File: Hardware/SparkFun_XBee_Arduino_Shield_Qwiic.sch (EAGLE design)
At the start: 76 parts, among them J4 QWIIC_RIGHT_ANGLE, Q1 220mA/50V/3.5Ω, Q3 3.1A/30V/105mΩ, Q5 20V/4.2A/52mΩ/1.4W, U1 FSUSB30MUX_MSOP10, U2 AP63203, U3 ESD Diode, U4 FT231XS, U5 ESD Diode, X1 JUMPER-SMT_2_NO_SILK

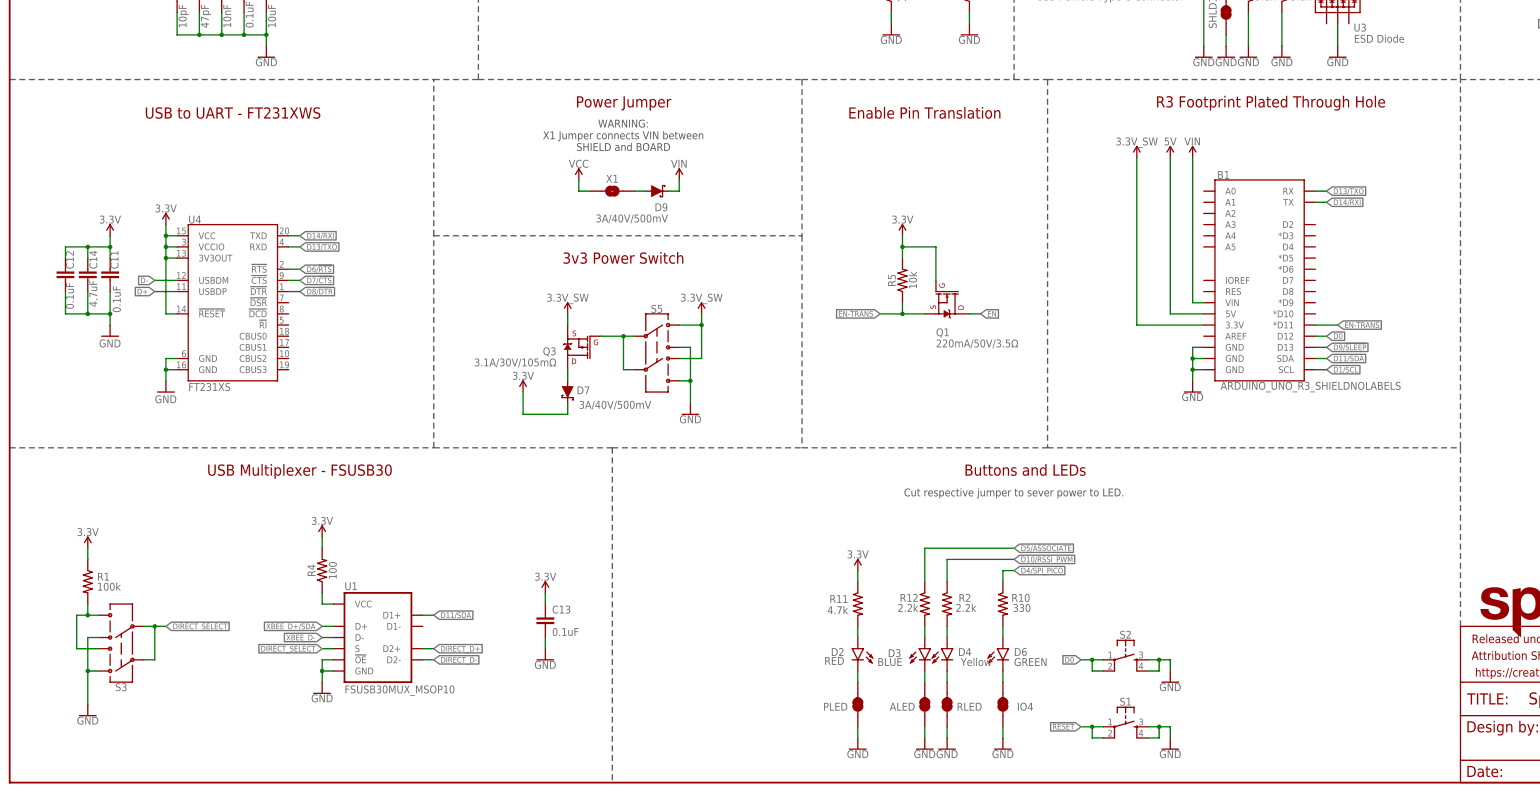
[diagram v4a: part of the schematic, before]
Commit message: Adds more measures and additional notes in the schematic
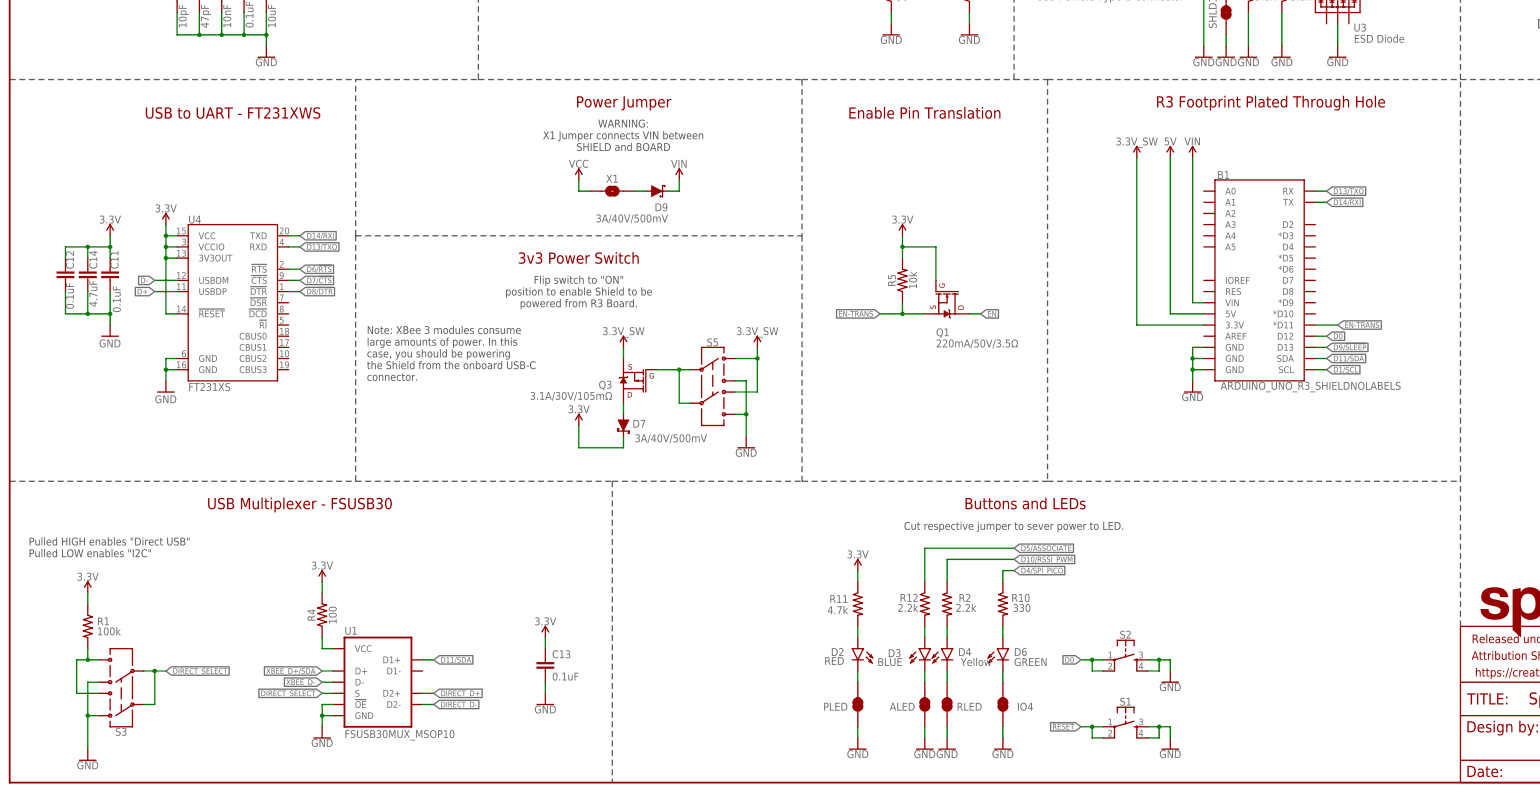
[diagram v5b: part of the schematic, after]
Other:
- note added: "Flip switch to "ON" position to enable Shield to be powered from R3 Board."
- note added: "Note: XBee 3 modules consume large amounts of power. In this case, you should be powering the Shield from the onboard USB-C connector."
- note added: "Pulled HIGH enables "Direct USB" Pulled LOW enables "I2C""
- moved on the sheet: C13, D7, Q3, R1, R4, S3, S5, U1

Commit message: Adds more measures, vias, and notes
* Rolls version to v10
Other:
- note added: "Flip the switch to the "ON" position to allow the XBee Shield to be powered from R3 Board."
- note added: "Note: Some XBee 3 modules, namely those with GNSS and LTE capabilites, consume more power than is possible to be provided through this switch. Use the onboard USB-C connector in this case."
- note added: "RF Module - XBee Module"
- note added: "VCC Range: 2.7V - 5.5V Check Datasheet for your specific module."
- note added: "v10"
- note removed: "Flip switch to "ON" position to enable Shield to be powered from R3 Board."
- note removed: "Note: XBee 3 modules consume large amounts of power. In this case, you should be powering the Shield from the onboard USB-C connector."
- note removed: "RF Module - XBee 3 Cat 1 Smart Modem"
- note removed: "VCC Range: 3.3V - 4.3V"
- note removed: "v03"
- moved on the sheet: D9, X1
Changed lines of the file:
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@@
 <sheet>
 <plain>
-<text x="48.26" y="266.7" size="1.778" layer="97" font="vector" align="center">VCC Range: 3.3V - 4.3V</text>
+<text x="50.8" y="264.16" size="1.778" layer="97" font="vector" align="center">VCC Range: 2.7V - 5.5V
+Check Datasheet for your specific module.</text>
 <text x="167.894" y="274.066" size="2.54" layer="94" font="vector" align="center">Buck Converter - AP63203</text>
 <text x="378.46" y="208.28" size="2.54" layer="94" font="vector" align="center">Qwiic - I2C</text>
-<text x="424.18" y="7.62" size="2.54" layer="94" font="vector" align="center">v03</text>
+<text x="424.18" y="7.62" size="2.54" layer="94" font="vector" align="center">v10</text>
 <text x="363.22" y="10.16" size="2.54" layer="94" font="vector" align="center">Elias Santistevan</text>
 <text x="231.14" y="63.5" size="2.54" layer="94" font="vector" align="center">Buttons and LEDs</text>
@@
 <text x="378.46" y="203.2" size="1.778" layer="97" font="vector" align="center">Cut I2C jumper to remove pullups.</text>
 <text x="228.6" y="58.42" size="1.778" layer="97" font="vector" align="center">Cut respective jumper to sever power to LED.</text>
-<text x="50.8" y="271.78" size="2.54" layer="94" font="vector" align="center">RF Module - XBee 3 Cat 1 Smart Modem</text>
+<text x="50.8" y="271.78" size="2.54" layer="94" font="vector" align="center">RF Module - XBee Module</text>
 <text x="378.46" y="269.24" size="2.54" layer="94" font="vector" align="center">0.1" Headers</text>
 <text x="241.046" y="208.788" size="1.778" layer="97" font="vector">Cut SHLD/SHLD1 jumper to disconnect
@@
 <text x="281.94" y="269.24" size="1.778" layer="97" font="vector" align="center">Use "UART" USB-C for general operation. </text>
 <text x="281.94" y="266.7" size="1.778" layer="97" font="vector" align="center">Use "Direct USB" USB-C for Cellular Firmware Updates</text>
-<text x="139.7" y="154.94" size="2.54" layer="94" font="vector" align="center">Power Jumper </text>
+<text x="127" y="154.94" size="2.54" layer="94" font="vector" align="center">Power Jumper </text>
 <text x="167.64" y="269.24" size="1.778" layer="97" font="vector" align="center">VIN R3: 7-15V</text>
 <wire x1="78.74" y1="124.46" x2="78.74" y2="160.02" width="0.2032" layer="97" style="longdash"/>
@@
 <text x="129.54" y="119.38" size="2.54" layer="94" font="vector" align="center">3v3 Power Switch</text>
 <wire x1="78.74" y1="124.46" x2="180.34" y2="124.46" width="0.2032" layer="97" style="longdash"/>
-<text x="139.7" y="147.32" size="1.778" layer="97" font="vector" align="center">WARNING:
+<text x="127" y="147.32" size="1.778" layer="97" font="vector" align="center">WARNING:
 X1 Jumper connects VIN between
 SHIELD and BOARD</text>
 <wire x1="330.2" y1="215.9" x2="431.8" y2="215.9" width="0.2032" layer="97" style="longdash"/>
-<text x="129.54" y="111.76" size="1.778" layer="97" font="vector" align="center">Flip switch to "ON"
-position to enable Shield to be
+<text x="129.54" y="111.76" size="1.778" layer="97" font="vector" align="center">Flip the switch to the "ON"
+position to allow the XBee Shield to be
 powered from R3 Board. </text>
-<text x="81.28" y="91.44" size="1.778" layer="97" font="vector">Note: XBee 3 modules consume
-large amounts of power. In this
-case, you should be powering
-the Shield from the onboard USB-C
-connector. </text>
+<text x="81.28" y="71.12" size="1.778" layer="97" font="vector">Note: Some XBee 3 modules, namely
+those with GNSS and LTE capabilites,
+consume more power than is possible
+to be provided through this switch.
+Use the onboard USB-C connector in this case.</text>
 <text x="4.318" y="51.308" size="1.778" layer="97" font="vector">Pulled HIGH enables "Direct USB"
 Pulled LOW enables "I2C"</text>
@@
 <attribute name="VALUE" x="142.24" y="79.248" size="1.778" layer="96" font="vector" align="top-left"/>
 </instance>
-<instance part="X1" gate="G$1" x="137.16" y="134.62" smashed="yes">
-<attribute name="NAME" x="137.16" y="137.414" size="1.778" layer="95" font="vector" align="center"/>
-</instance>
-<instance part="D9" gate="G$1" x="147.32" y="134.62" smashed="yes">
-<attribute name="NAME" x="149.86" y="131.826" size="1.778" layer="95" font="vector" rot="R180"/>
-<attribute name="VALUE" x="149.86" y="127.508" size="1.778" layer="96" font="vector" rot="R180" align="top-left"/>
-</instance>
-<instance part="SUPPLY2" gate="G$1" x="129.54" y="137.16" smashed="yes">
-<attribute name="VALUE" x="129.54" y="139.954" size="1.778" layer="96" font="vector" align="bottom-center"/>
-</instance>
-<instance part="SUPPLY5" gate="G$1" x="152.4" y="137.16" smashed="yes">
-<attribute name="VALUE" x="152.4" y="139.954" size="1.778" layer="96" font="vector" align="bottom-center"/>
+<instance part="X1" gate="G$1" x="124.46" y="134.62" smashed="yes">
+<attribute name="NAME" x="124.46" y="137.414" size="1.778" layer="95" font="vector" align="center"/>
+</instance>
+<instance part="D9" gate="G$1" x="134.62" y="134.62" smashed="yes">
+<attribute name="NAME" x="137.16" y="131.826" size="1.778" layer="95" font="vector" rot="R180"/>
+<attribute name="VALUE" x="137.16" y="127.508" size="1.778" layer="96" font="vector" rot="R180" align="top-left"/>
+</instance>
+<instance part="SUPPLY2" gate="G$1" x="116.84" y="137.16" smashed="yes">
+<attribute name="VALUE" x="116.84" y="139.954" size="1.778" layer="96" font="vector" align="bottom-center"/>
+</instance>
+<instance part="SUPPLY5" gate="G$1" x="139.7" y="137.16" smashed="yes">
+<attribute name="VALUE" x="139.7" y="139.954" size="1.778" layer="96" font="vector" align="bottom-center"/>
 </instance>
 <instance part="SUPPLY21" gate="G$1" x="269.24" y="142.24" smashed="yes">
@@
 <segment>
 <pinref part="D9" gate="G$1" pin="C"/>
-<wire x1="152.4" y1="134.62" x2="149.86" y2="134.62" width="0.1524" layer="91"/>
+<wire x1="139.7" y1="134.62" x2="137.16" y2="134.62" width="0.1524" layer="91"/>
 <pinref part="SUPPLY5" gate="G$1" pin="VIN"/>
-<wire x1="152.4" y1="134.62" x2="152.4" y2="137.16" width="0.1524" layer="91"/>
+<wire x1="139.7" y1="134.62" x2="139.7" y2="137.16" width="0.1524" layer="91"/>
 </segment>
 </net>
@@
 <segment>
 <pinref part="X1" gate="G$1" pin="1"/>
-<wire x1="132.08" y1="134.62" x2="129.54" y2="134.62" width="0.1524" layer="91"/>
-<wire x1="129.54" y1="134.62" x2="129.54" y2="137.16" width="0.1524" layer="91"/>
+<wire x1="119.38" y1="134.62" x2="116.84" y2="134.62" width="0.1524" layer="91"/>
+<wire x1="116.84" y1="134.62" x2="116.84" y2="137.16" width="0.1524" layer="91"/>
 <pinref part="SUPPLY2" gate="G$1" pin="VCC"/>
 </segment>
@@
 <pinref part="X1" gate="G$1" pin="2"/>
 <pinref part="D9" gate="G$1" pin="A"/>
-<wire x1="142.24" y1="134.62" x2="144.78" y2="134.62" width="0.1524" layer="91"/>
-</segment>
-</net>
+<wire x1="129.54" y1="134.62" x2="132.08" y2="134.62" width="0.1524" layer="91"/>
+</segment>
+</net>

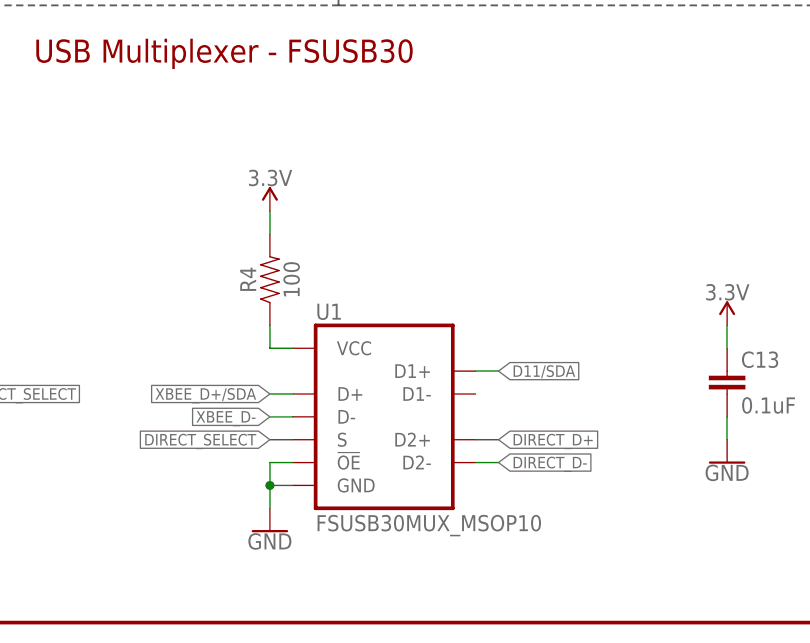
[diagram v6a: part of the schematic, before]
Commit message: Replaces old USB mux switch with new one
* Removes 100Ohm resistor on VCC line
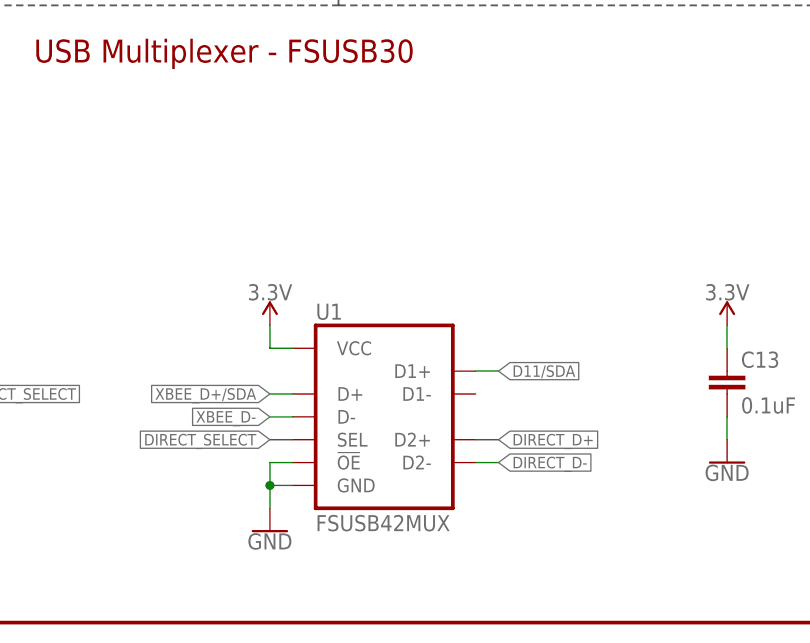
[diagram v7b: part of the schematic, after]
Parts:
- removed R4: 100, SparkFun-Resistors:100OHM-0603-1/10W-1%
- U1: value FSUSB30MUX_MSOP10 -> FSUSB42MUX; device SparkFun-IC-Special-Function:FSUSB30MUX_MSOP10 -> SparkFun-IC-Special-Function:FSUSB42MUX
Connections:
- removed net N$10: R4.1, U1.VCC
- net 3.3V: now also U1.VCC; no longer R4.2
- net DIRECT_SELECT: now also U1.SEL; no longer U1.S
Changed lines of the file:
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@@
 <part name="B1" library="SparkFun-Boards" deviceset="ARDUINO_UNO_R3_SHIELD" device="NOLABELS"/>
 <part name="GND5" library="SparkFun-PowerSymbols" deviceset="GND" device=""/>
-<part name="U1" library="SparkFun-IC-Special-Function" deviceset="FSUSB30MUX" device="_MSOP10"/>
 <part name="GND29" library="SparkFun-PowerSymbols" deviceset="GND" device=""/>
 <part name="SUPPLY12" library="SparkFun-PowerSymbols" deviceset="3.3V" device=""/>
@@
 <part name="C8" library="SparkFun-Capacitors" deviceset="10PF" device="-0603-50V-5%" value="10pF"/>
 <part name="C13" library="SparkFun-Capacitors" deviceset="0.1UF" device="-0603-25V-(+80/-20%)" value="0.1uF"/>
-<part name="R4" library="SparkFun-Resistors" deviceset="100OHM" device="-0603-1/10W-1%" value="100"/>
 <part name="GND9" library="SparkFun-PowerSymbols" deviceset="GND" device=""/>
 <part name="SUPPLY17" library="SparkFun-PowerSymbols" deviceset="3.3V" device=""/>
@@
 <part name="R5" library="SparkFun-Resistors" deviceset="10KOHM" device="-0603-1/10W-1%" value="10k"/>
 <part name="SUPPLY27" library="SparkFun-PowerSymbols" deviceset="3.3V" device=""/>
+<part name="U1" library="SparkFun-IC-Special-Function" deviceset="FSUSB42MUX" device=""/>
 </parts>
 <sheets>
@@
 <attribute name="VALUE" x="269.24" y="88.646" size="1.778" layer="96" font="vector" align="top-center"/>
 </instance>
-<instance part="U1" gate="U1" x="83.82" y="22.86" smashed="yes">
-<attribute name="NAME" x="76.2" y="33.655" size="1.778" layer="95" font="vector"/>
-<attribute name="VALUE" x="76.2" y="10.16" size="1.778" layer="96" font="vector"/>
-</instance>
 <instance part="GND29" gate="1" x="71.12" y="10.16" smashed="yes" rot="MR0">
 <attribute name="VALUE" x="71.12" y="9.906" size="1.778" layer="96" font="vector" rot="MR0" align="top-center"/>
 </instance>
-<instance part="SUPPLY12" gate="G$1" x="71.12" y="45.72" smashed="yes" rot="MR0">
-<attribute name="VALUE" x="71.12" y="48.514" size="1.778" layer="96" font="vector" rot="MR0" align="bottom-center"/>
+<instance part="SUPPLY12" gate="G$1" x="71.12" y="33.02" smashed="yes" rot="MR0">
+<attribute name="VALUE" x="71.12" y="35.814" size="1.778" layer="96" font="vector" rot="MR0" align="bottom-center"/>
 </instance>
 <instance part="S3" gate="G$1" x="25.4" y="20.32" smashed="yes" rot="R180">
@@
 <attribute name="NAME" x="123.444" y="28.321" size="1.778" layer="95" font="vector"/>
 <attribute name="VALUE" x="123.444" y="23.241" size="1.778" layer="96" font="vector"/>
-</instance>
-<instance part="R4" gate="G$1" x="71.12" y="38.1" smashed="yes" rot="R90">
-<attribute name="NAME" x="69.596" y="38.1" size="1.778" layer="95" font="vector" rot="R90" align="bottom-center"/>
-<attribute name="VALUE" x="72.644" y="38.1" size="1.778" layer="96" font="vector" rot="R90" align="top-center"/>
 </instance>
 <instance part="GND9" gate="1" x="121.92" y="17.78" smashed="yes" rot="MR0">
@@
 <attribute name="VALUE" x="203.2" y="127.254" size="1.778" layer="96" font="vector" rot="MR0" align="bottom-center"/>
 </instance>
+<instance part="U1" gate="G$1" x="83.82" y="22.86" smashed="yes">
+<attribute name="NAME" x="76.2" y="33.655" size="1.778" layer="95" font="vector"/>
+<attribute name="VALUE" x="76.2" y="10.16" size="1.778" layer="96" font="vector"/>
+</instance>
 </instances>
 <busses>
@@
 </segment>
 <segment>
-<pinref part="U1" gate="U1" pin="D1+"/>
 <wire x1="96.52" y1="27.94" x2="93.98" y2="27.94" width="0.1524" layer="91"/>
 <label x="96.52" y="27.94" size="1.27" layer="95" font="vector" xref="yes"/>
+<pinref part="U1" gate="G$1" pin="D1+"/>
 </segment>
 <segment>
@@
 </segment>
 <segment>
-<pinref part="U1" gate="U1" pin="GND"/>
 <wire x1="71.12" y1="12.7" x2="71.12" y2="15.24" width="0.1524" layer="91"/>
 <wire x1="71.12" y1="15.24" x2="73.66" y2="15.24" width="0.1524" layer="91"/>
 <pinref part="GND29" gate="1" pin="GND"/>
-<pinref part="U1" gate="U1" pin="!OE!"/>
 <wire x1="73.66" y1="17.78" x2="71.12" y2="17.78" width="0.1524" layer="91"/>
 <wire x1="71.12" y1="17.78" x2="71.12" y2="15.24" width="0.1524" layer="91"/>
 <junction x="71.12" y="15.24"/>
+<pinref part="U1" gate="G$1" pin="GND"/>
+<pinref part="U1" gate="G$1" pin="!OE!"/>
 </segment>
 <segment>
@@
 </segment>
 <segment>
-<pinref part="R4" gate="G$1" pin="2"/>
 <pinref part="SUPPLY12" gate="G$1" pin="3.3V"/>
-<wire x1="71.12" y1="43.18" x2="71.12" y2="45.72" width="0.1524" layer="91"/>
+<wire x1="71.12" y1="30.48" x2="73.66" y2="30.48" width="0.1524" layer="91"/>
+<pinref part="U1" gate="G$1" pin="VCC"/>
+<wire x1="71.12" y1="30.48" x2="71.12" y2="33.02" width="0.1524" layer="91"/>
 </segment>
 <segment>
@@
 <net name="XBEE_D+/SDA" class="2">
 <segment>
-<pinref part="U1" gate="U1" pin="D+"/>
 <wire x1="71.12" y1="25.4" x2="73.66" y2="25.4" width="0.1524" layer="91"/>
 <label x="71.12" y="25.4" size="1.27" layer="95" font="vector" rot="R180" xref="yes"/>
+<pinref part="U1" gate="G$1" pin="D+"/>
 </segment>
 <segment>
@@
 <net name="XBEE_D-" class="2">
 <segment>
-<pinref part="U1" gate="U1" pin="D-"/>
 <wire x1="71.12" y1="22.86" x2="73.66" y2="22.86" width="0.1524" layer="91"/>
 <label x="71.12" y="22.86" size="1.27" layer="95" font="vector" rot="R180" xref="yes"/>
+<pinref part="U1" gate="G$1" pin="D-"/>
 </segment>
 <segment>
@@
 <net name="DIRECT_D+" class="2">
 <segment>
-<pinref part="U1" gate="U1" pin="D2+"/>
 <wire x1="96.52" y1="20.32" x2="93.98" y2="20.32" width="0.1524" layer="91"/>
 <label x="96.52" y="20.32" size="1.27" layer="95" font="vector" xref="yes"/>
+<pinref part="U1" gate="G$1" pin="D2+"/>
 </segment>
 <segment>
@@
 <net name="DIRECT_D-" class="2">
 <segment>
-<pinref part="U1" gate="U1" pin="D2-"/>
 <wire x1="96.52" y1="17.78" x2="93.98" y2="17.78" width="0.1524" layer="91"/>
 <label x="96.52" y="17.78" size="1.27" layer="95" font="vector" xref="yes"/>
+<pinref part="U1" gate="G$1" pin="D2-"/>
 </segment>
 <segment>
@@
 <net name="DIRECT_SELECT" class="0">
 <segment>
-<pinref part="U1" gate="U1" pin="S"/>
 <wire x1="73.66" y1="20.32" x2="71.12" y2="20.32" width="0.1524" layer="91"/>
 <label x="71.12" y="20.32" size="1.27" layer="95" font="vector" rot="R180" xref="yes"/>
+<pinref part="U1" gate="G$1" pin="SEL"/>
 </segment>
 <segment>
@@
 </segment>
 </net>
-<net name="N$10" class="0">
-<segment>
-<pinref part="U1" gate="U1" pin="VCC"/>
-<wire x1="71.12" y1="30.48" x2="73.66" y2="30.48" width="0.1524" layer="91"/>
-<pinref part="R4" gate="G$1" pin="1"/>
-<wire x1="71.12" y1="30.48" x2="71.12" y2="33.02" width="0.1524" layer="91"/>
-</segment>
-</net>
